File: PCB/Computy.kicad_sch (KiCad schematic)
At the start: 44 parts, among them J1 USB_C_Receptacle_USB2.0_16P, J2 Conn_ARM_JTAG_SWD_10, J3 Conn_01x03_Socket, J4 Conn_01x04_Socket, J5 Conn_02x04_Odd_Even, M1 Motor_Servo, M2 Motor_Servo, M3 Motor_Servo, M4 Motor_Servo, M5 Motor_Servo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

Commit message: Computy v2
- Fix issues with the PCB
    - Connect SWO
    - Connect CC1101 to SPI1
    - Fix BNO055 SCL and SDA
    - Add more testpoints
- Update firmware
- Add most recent datasheets
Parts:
- added TP4: TP_SDA, TestPoint:TestPoint_THTPad_2.0x2.0mm_Drill1.0mm, symbol Connector:TestPoint_Probe
- added TP5: TP_SCL, TestPoint:TestPoint_THTPad_2.0x2.0mm_Drill1.0mm, symbol Connector:TestPoint_Probe
- H1, H2, H3, H4: footprint MountingHole:MountingHole_3.2mm_M3 -> MountingHole:MountingHole_3.2mm_M3_DIN965_Pad
- R3, R4: value 10k -> 4.7k
- TP1: value TestPoint_Probe -> TP_5V; footprint TestPoint:TestPoint_THTPad_1.0x1.0mm_Drill0.5mm -> TestPoint:TestPoint_THTPad_2.0x2.0mm_Drill1.0mm
- TP2: value TestPoint_Probe -> TP_3.3V; footprint TestPoint:TestPoint_THTPad_1.0x1.0mm_Drill0.5mm -> TestPoint:TestPoint_THTPad_2.0x2.0mm_Drill1.0mm
- TP3: value TestPoint_Probe -> TestPoint_GND; footprint TestPoint:TestPoint_THTPad_1.0x1.0mm_Drill0.5mm -> TestPoint:TestPoint_THTPad_2.0x2.0mm_Drill1.0mm
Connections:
- net CC1101_CSN: now also U1.58 (PB6); no longer U1.21 (PA5)
- net I2C2_SCL: now also U3.19 (COM1), TP5.1; no longer U3.20 (COM0)
- net I2C2_SDA: now also U3.20 (COM0), TP4.1; no longer U3.19 (COM1)
- net SWO: now reaches J2.6 (SWO/TDO)
- net SWO: now also U1.55 (PB3)
- net SPI3_MISO renamed SPI1_MISO
- net SPI3_MOSI renamed SPI1_MOSI
- net SPI3_SCK renamed SPI1_SCK
- net SPI1_SCK: now also U1.21 (PA5); no longer U1.55 (PB3)
- no-connect marks 7 -> 10
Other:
- note added: "I2C addr: 0x28"
- note removed: "Change to 4.7k"
- note removed: "Connect SWO for debugging"
- note removed: "Connect to GND"
- note removed: "Move to SPI1"
- note removed: "Those two have to be swapped! COM0 - SDA COM1 - SCL"
- moved on the sheet: H1, H2, H3, H4, TP1, TP2, TP3

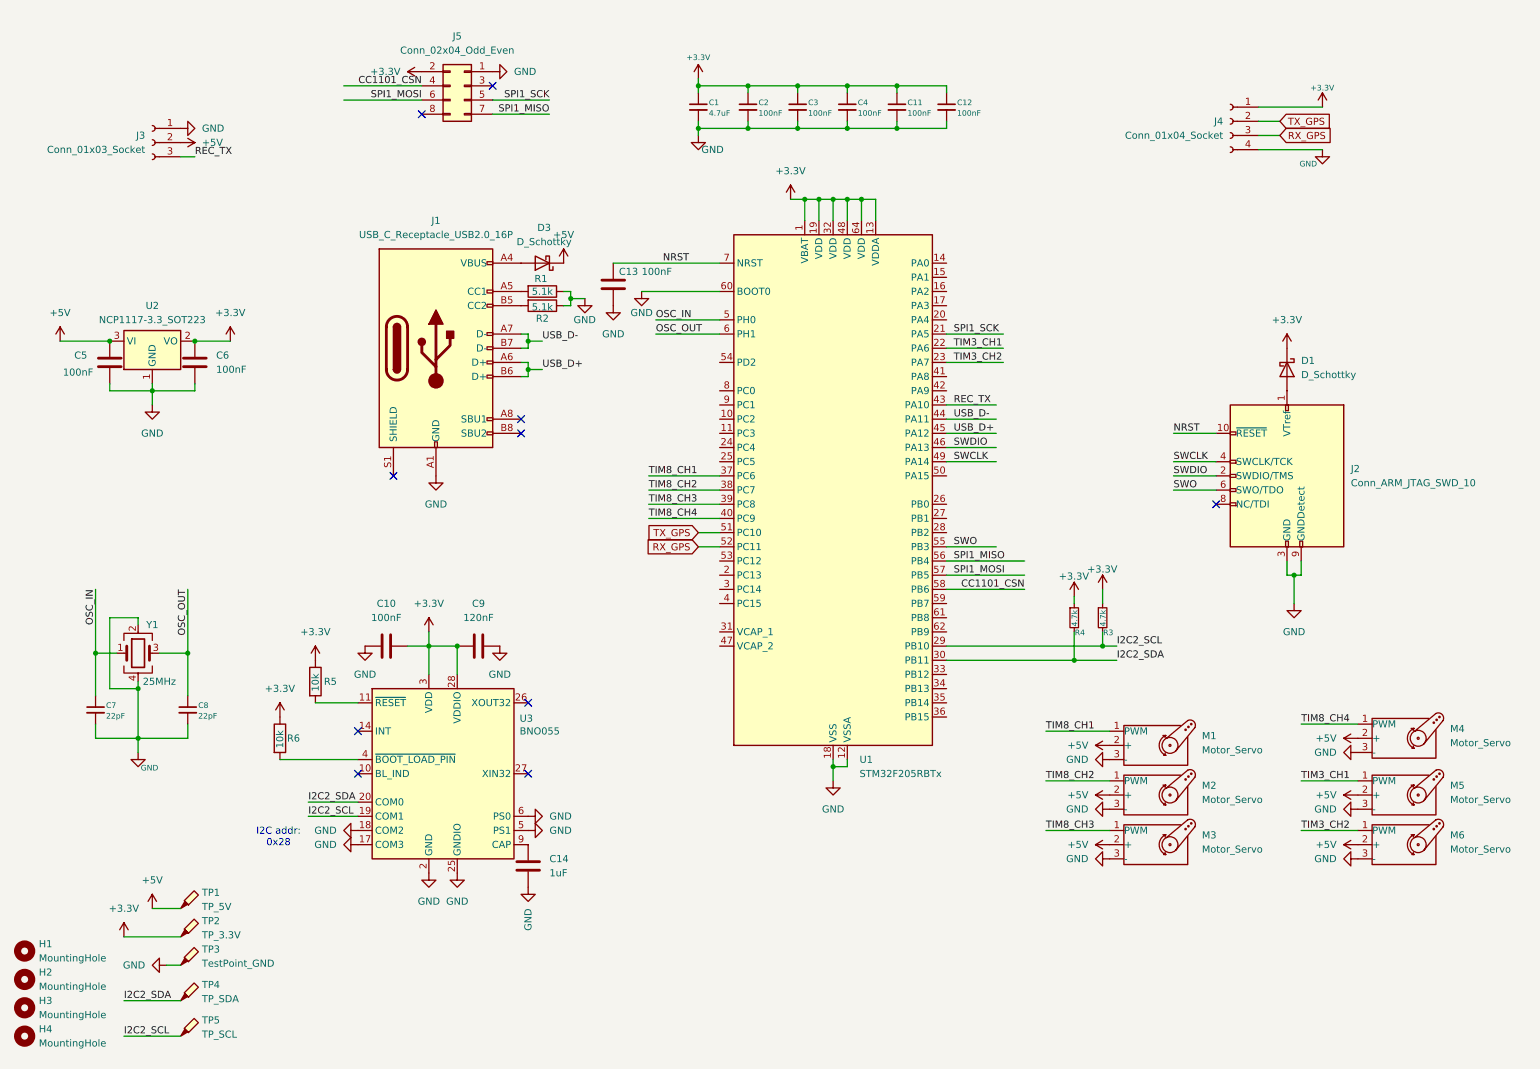
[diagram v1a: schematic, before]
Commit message: Add DF13 connector for GPS and telemetry
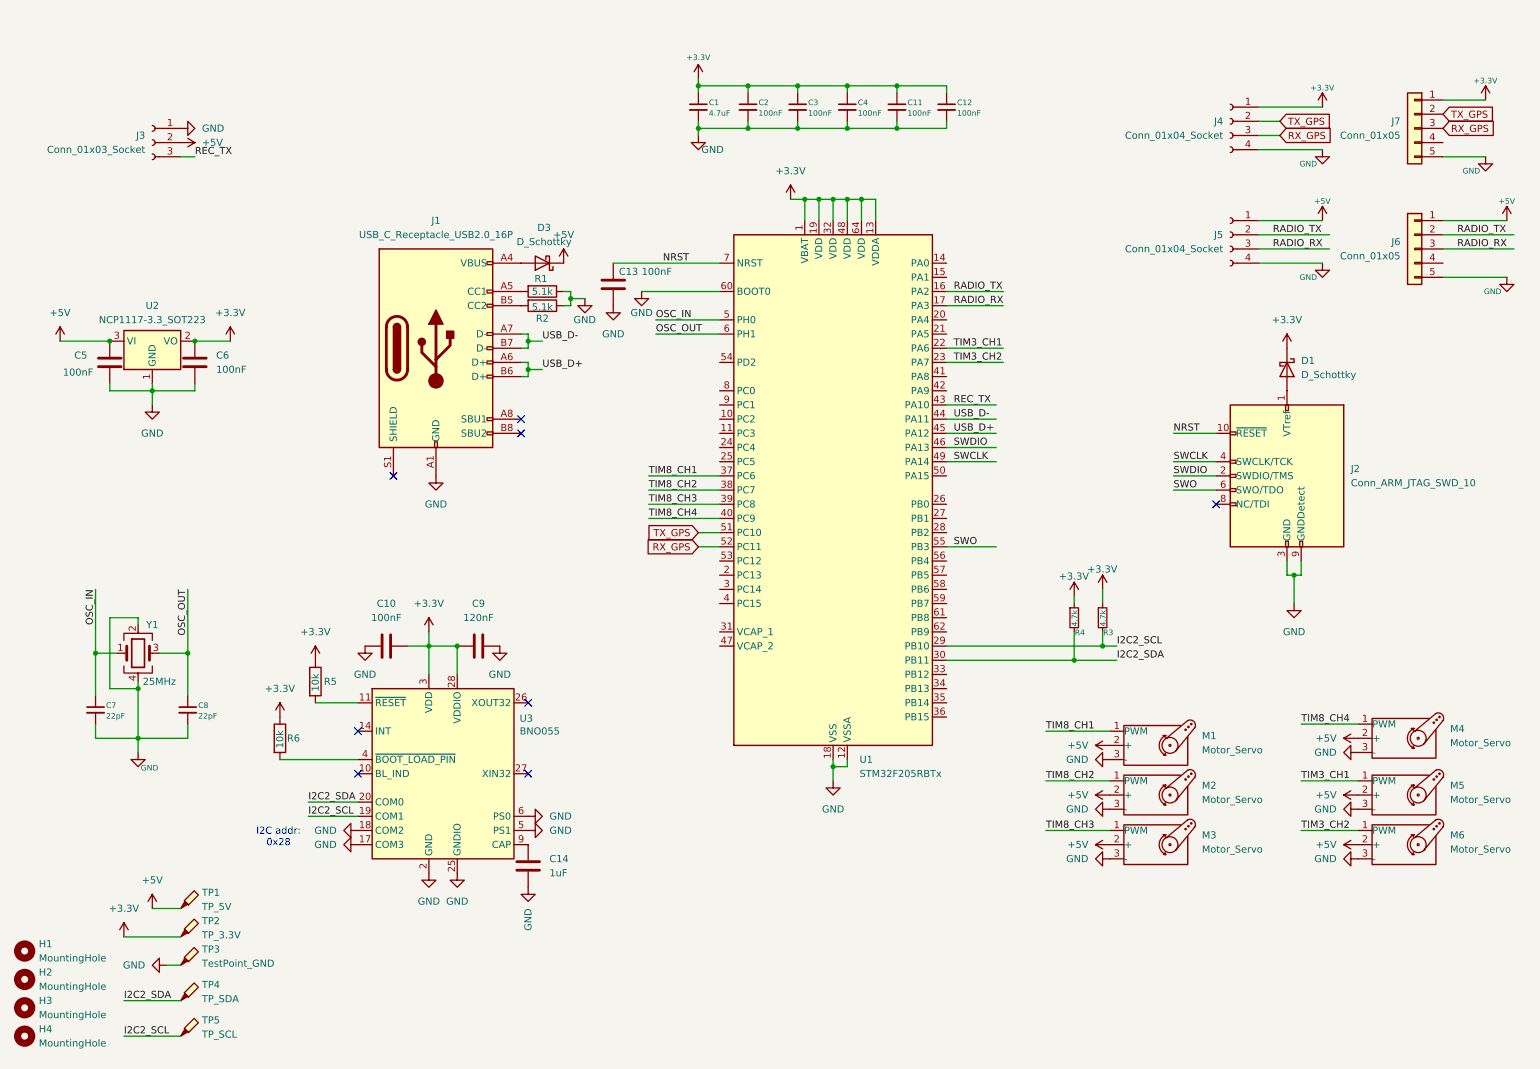
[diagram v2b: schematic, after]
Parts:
- removed J5: Conn_02x04_Odd_Even, Connector_PinSocket_2.54mm:PinSocket_2x04_P2.54mm_Vertical, symbol Connector_Generic:Conn_02x04_Odd_Even
- added J5: Conn_01x04_Socket, Connector_PinSocket_2.54mm:PinSocket_1x04_P2.54mm_Vertical, symbol Connector:Conn_01x04_Socket
- added J6, J7: Conn_01x05, Connector_Hirose:Hirose_DF13-05P-1.25DSA_1x05_P1.25mm_Vertical, symbol Connector_Generic:Conn_01x05
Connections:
- net +3.3V: now also J7.1 (Pin_1)
- net +5V: now also J5.1 (Pin_1), J6.1 (Pin_1)
- net GND: now also J5.4 (Pin_4), J6.5 (Pin_5), J7.5 (Pin_5)
- net RX_GPS: now also J7.3 (Pin_3)
- net TX_GPS: now also J7.2 (Pin_2)
- net RADIO_TX: now reaches U1.16 (PA2)
- net RADIO_TX: now also J5.2 (Pin_2), J6.2 (Pin_2)
- net RADIO_RX: now reaches U1.17 (PA3)
- net RADIO_RX: now also J5.3 (Pin_3), J6.3 (Pin_3)
- net CC1101_CSN: no longer names the net of U1.58 (PB6)
- net SPI1_MISO: no longer names the net of U1.56 (PB4)
- net SPI1_MOSI: no longer names the net of U1.57 (PB5)
- net SPI1_SCK: no longer names the net of U1.21 (PA5)
- no-connect marks 10 -> 8

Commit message: Add LED to board
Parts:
- added D2, D4: LED, LED_SMD:LED_0805_2012Metric_Pad1.15x1.40mm_HandSolder, symbol Device:LED
- added R7, R8: 220, Resistor_SMD:R_0805_2012Metric_Pad1.20x1.40mm_HandSolder, symbol Device:R
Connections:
- net +3.3V: now also R7.2
- net GND: now also D2.1 (K), D4.1 (K)
- net LED_MCU: now reaches U1.8 (PC0)
- net LED_MCU: now also R8.2
- new net: D2.2 (A), R7.1
- new net: D4.2 (A), R8.1
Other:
- note added: "Power status LED"
- note added: "RGB controlled by STM32"

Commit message: Add CAN transceiver
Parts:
- added J8: Conn_01x04_Socket, Connector_PinHeader_2.54mm:PinHeader_1x04_P2.54mm_Vertical, symbol Connector:Conn_01x04_Socket
- added R10: 120, Resistor_SMD:R_0805_2012Metric_Pad1.20x1.40mm_HandSolder, symbol Device:R
- added R9: 10k, Resistor_SMD:R_0805_2012Metric_Pad1.20x1.40mm_HandSolder, symbol Device:R
- added U4: MCP2558FD-xSN, Package_SO:SOIC-8_3.9x4.9mm_P1.27mm, symbol Interface_CAN_LIN:MCP2558FD-xSN
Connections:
- net +5V: now also J8.1 (Pin_1), U4.3 (VDD)
- net GND: now also J8.4 (Pin_4), R9.2, U4.2 (VSS)
- net CAN2_TX: now reaches U1.33 (PB12)
- net CAN2_TX: now also U4.1 (TXD)
- net CAN2_RX: now reaches U1.34 (PB13)
- net CAN2_RX: now also U4.4 (RXD)
- new net: R9.1, U4.8 (S)
- new net CAN_H: J8.2 (Pin_2), R10.1, U4.7 (CANH)
- new net CAN_L: J8.3 (Pin_3), R10.2, U4.6 (CANL)

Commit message: PCB fixes
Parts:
- added C15, C16: 100nF, Capacitor_SMD:C_0805_2012Metric_Pad1.18x1.45mm_HandSolder, symbol Device:C
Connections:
- net +3.3V: now also U4.5 (VIO), C16.1
- net +5V: now also C15.1
- net CAN2_RX: now also U1.33 (PB12); no longer U1.34 (PB13)
- net CAN2_TX: now also U1.34 (PB13); no longer U1.33 (PB12)
- net GND: now also C15.2, C16.2

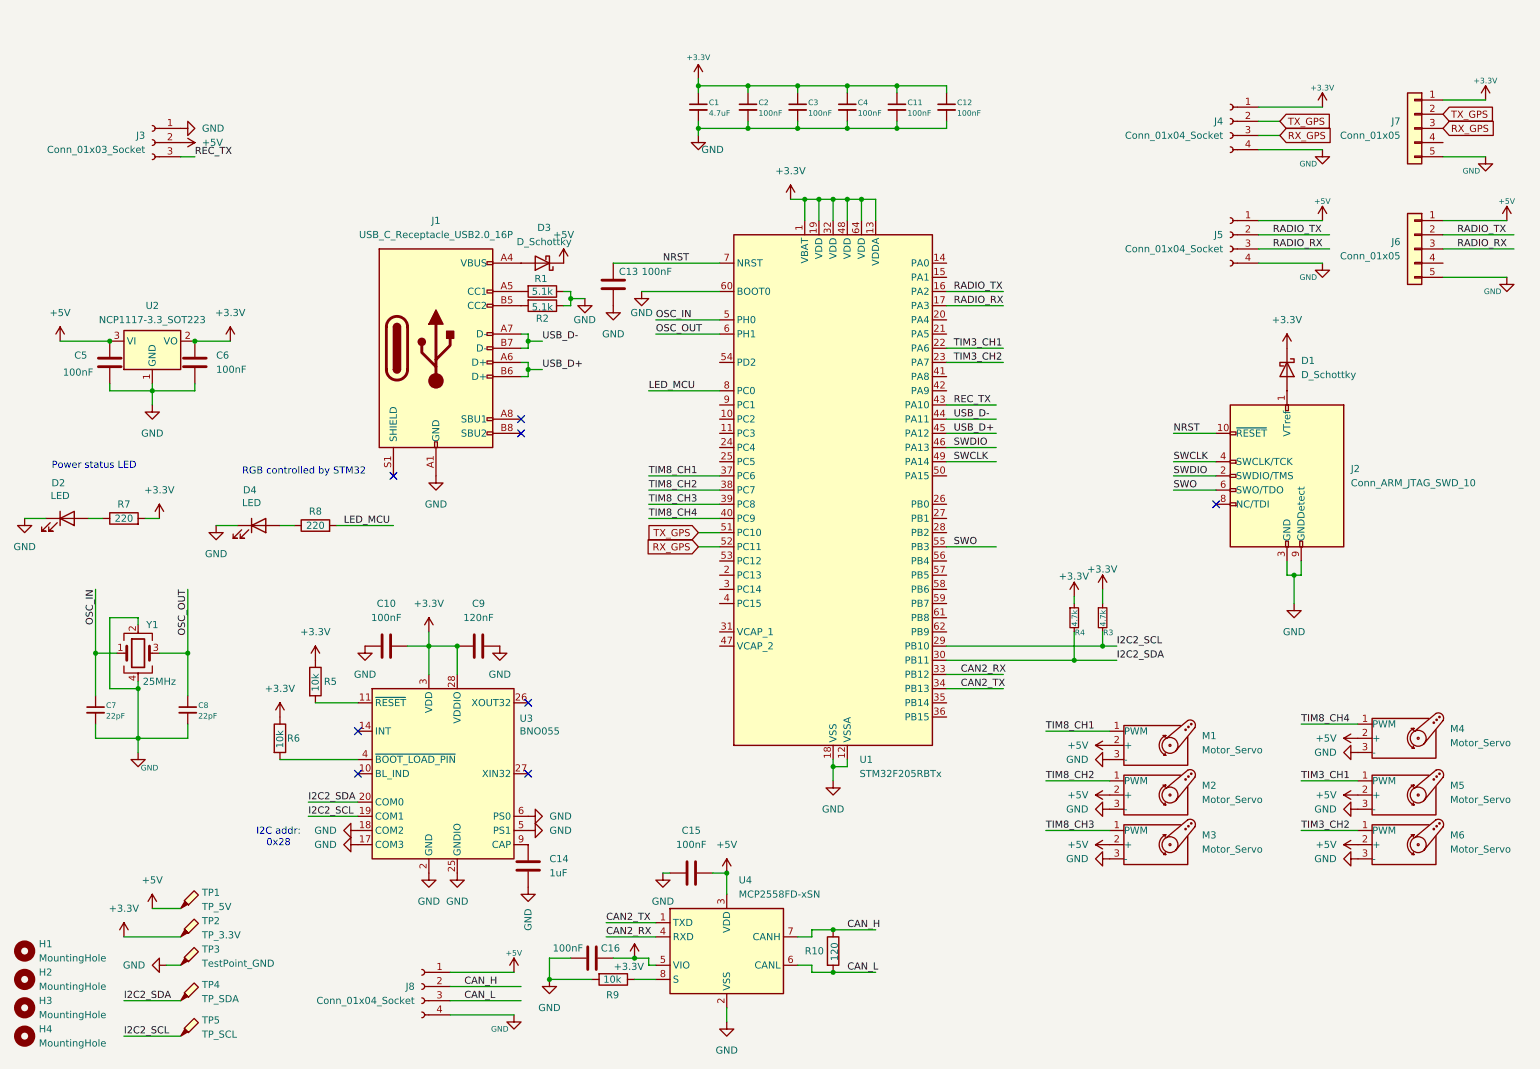
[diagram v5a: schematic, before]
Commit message: Expose UART5 and I2C2 on the PCB
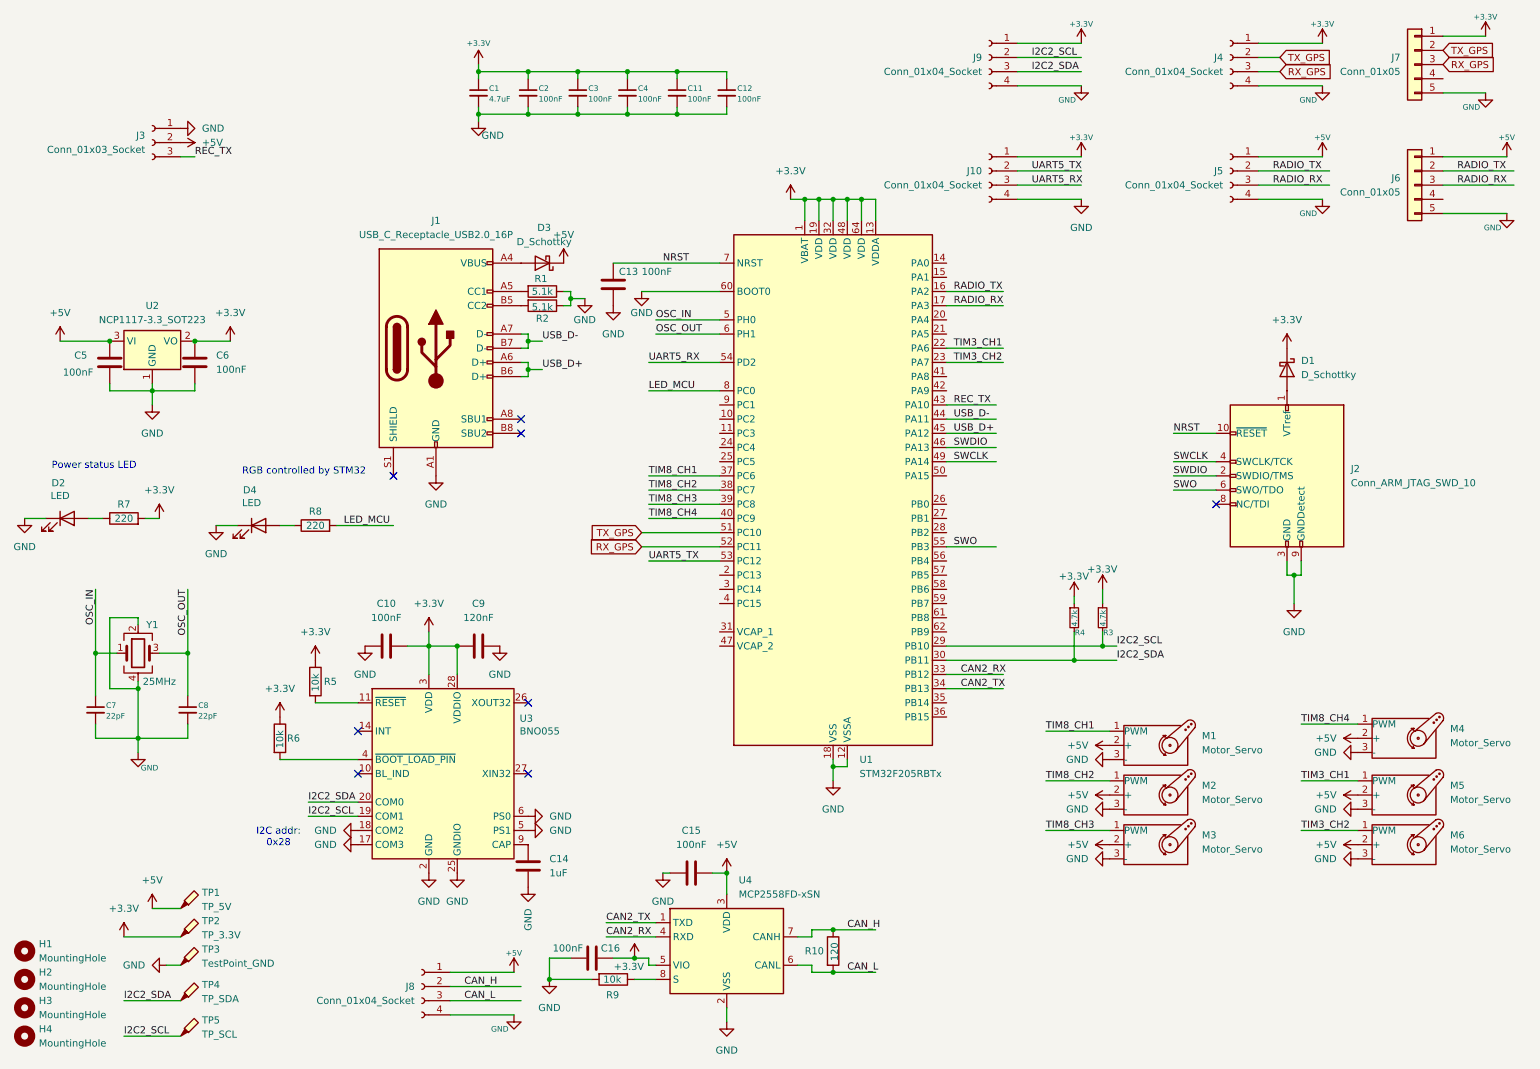
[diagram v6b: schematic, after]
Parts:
- added J10, J9: Conn_01x04_Socket, Connector_PinSocket_2.54mm:PinSocket_1x04_P2.54mm_Vertical, symbol Connector:Conn_01x04_Socket
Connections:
- net +3.3V: now also J10.1 (Pin_1), J9.1 (Pin_1)
- net GND: now also J10.4 (Pin_4), J9.4 (Pin_4)
- net I2C2_SCL: now also J9.2 (Pin_2)
- net I2C2_SDA: now also J9.3 (Pin_3)
- net UART5_TX: now reaches U1.53 (PC12)
- net UART5_TX: now also J10.2 (Pin_2)
- net UART5_RX: now reaches U1.54 (PD2)
- net UART5_RX: now also J10.3 (Pin_3)
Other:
- moved on the sheet: C1, C11, C12, C2, C3, C4, J4, J5, J6, J7
